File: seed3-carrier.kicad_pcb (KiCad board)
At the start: 2 copper layers, 113 x 61.6 mm, 47 parts, among them J1 AudioJack2, J2 AudioJack2, J3 5V_IN, J4 DISPLAY_UART, J5 SJ1-3535NG, J6 Seed3_PINS_RIGHT, J7 Seed3_PINS_LEFT, U1 TLV9062IDR, U2 TPA6111A2DR

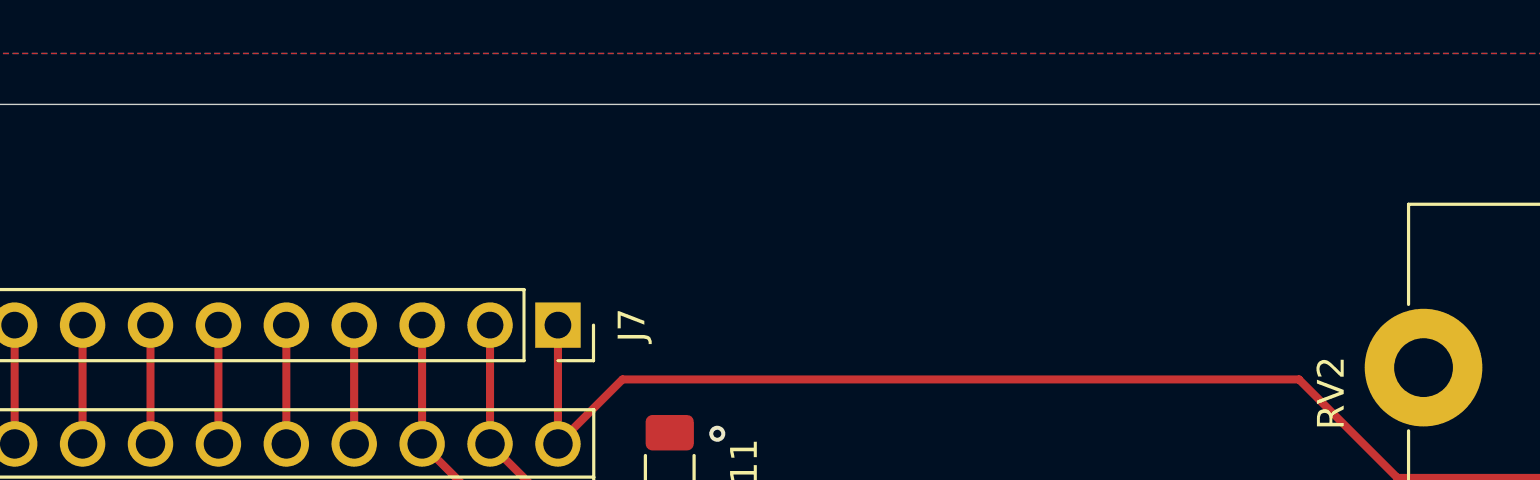
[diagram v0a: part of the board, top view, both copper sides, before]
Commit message: Add board revision, designer credits, and date to silkscreen
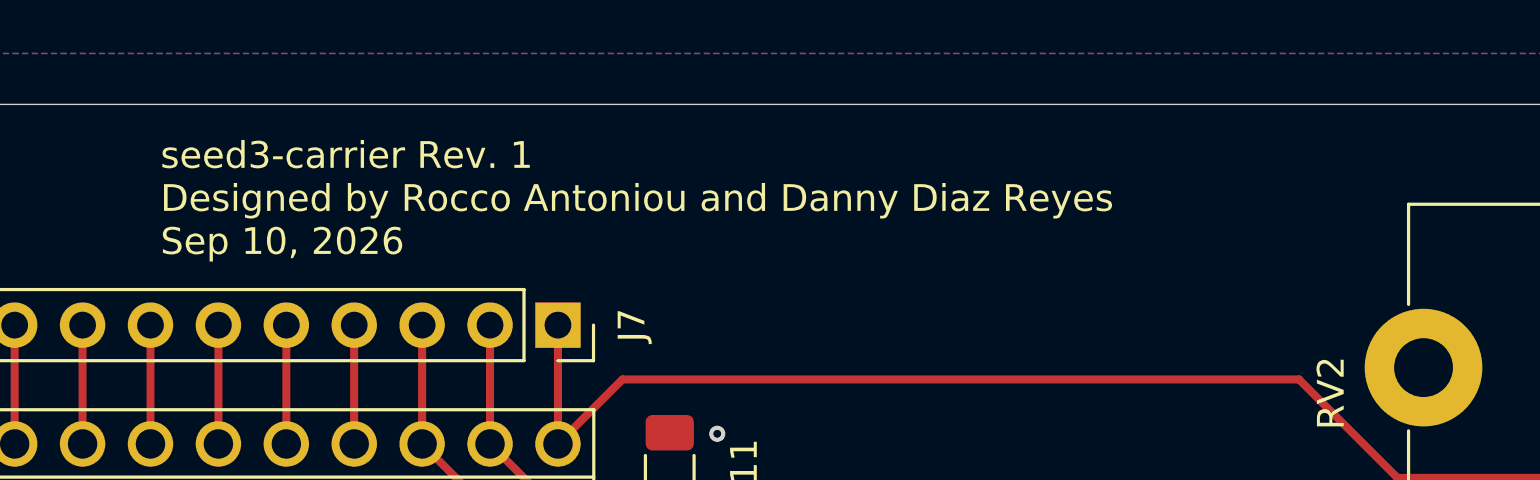
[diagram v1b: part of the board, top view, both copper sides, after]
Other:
- board text added: "seed3-carrier Rev. 1 Designed by Rocco Antoniou and Danny Diaz Reyes Sep 10, 2026"
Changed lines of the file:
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@@
+		)
+	)
+	(gr_text "seed3-carrier Rev. 1\nDesigned by Rocco Antoniou and Danny Diaz Reyes\nSep 10, 2026\n"
+		(at 86.106 45.72 0)
+		(layer "F.SilkS")
+		(effects
+			(font
+				(size 1 1)
+				(thickness 0.1)
+			)
+			(justify left bottom)
 		)
 	)

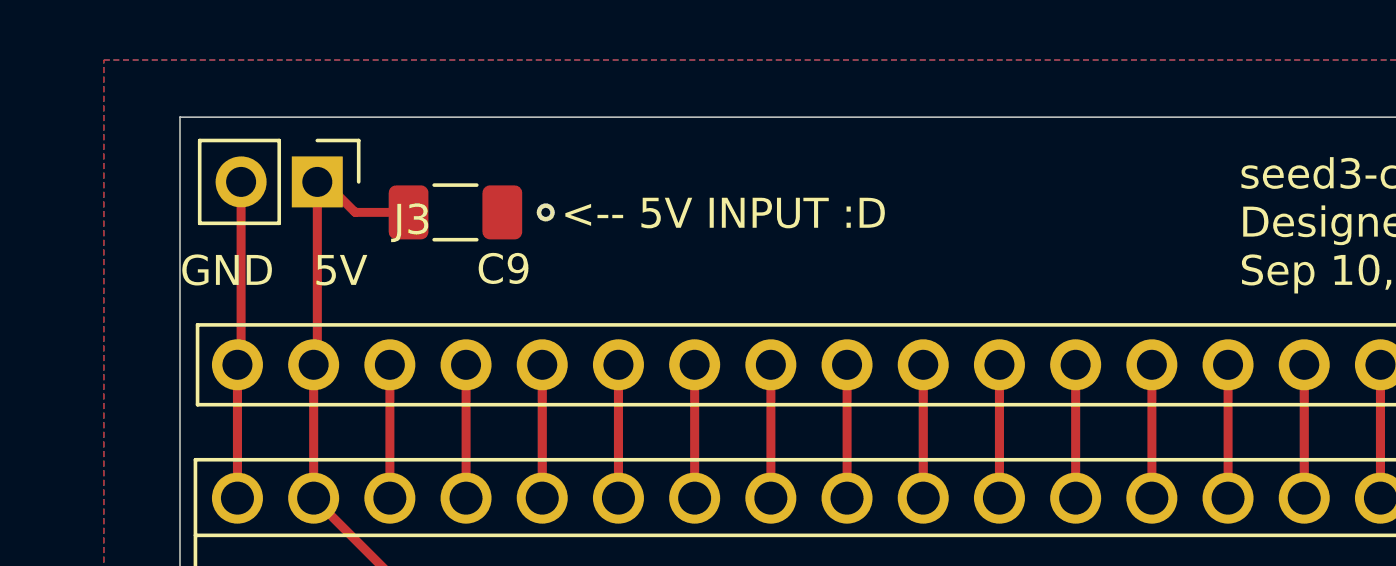
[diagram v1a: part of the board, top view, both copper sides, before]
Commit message: Add reverse-polarity protection and switched input mute
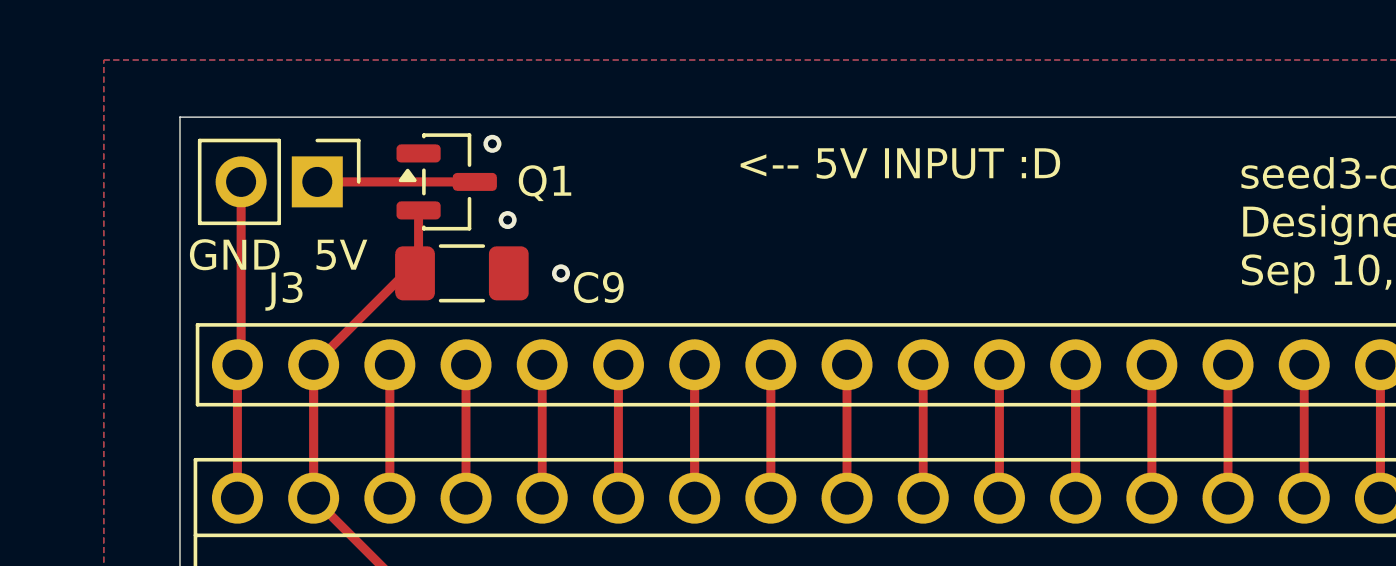
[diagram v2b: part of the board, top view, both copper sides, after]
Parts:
- added Q1: AO3401A, Package_TO_SOT_SMD:SOT-23, F.Cu at (59.7, 42.2)
- J1: value AudioJack2 -> AudioJack2_Switch
- moved C9 2.04 mm to (60.2, 45.2)
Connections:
- J1 pad SN: (no net) -> unconnected-(J1-PadSN)
- J1 pad TN: (no net) -> GND
- J3 pad 1: +5V -> Net-(J3-Pin_1)
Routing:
- net Net-(J3-Pin_1): track 0.00 -> 5.25 mm
- net +5V: track 132.6 -> 129.8 mm
- net GND: vias 16 -> 18

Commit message: Expand display header to four pins with protected 5V
Preserve GND and UART pin assignments and add protected +5V on pin 4. Reposition and label the header, reroute UART connections, and complete the power route with a short bottom-layer crossing beneath the buffered audio input. Refill copper zones.
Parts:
- J4: footprint Connector_PinHeader_2.54mm:PinHeader_1x03_P2.54mm_Vertical -> Connector_PinHeader_2.54mm:PinHeader_1x04_P2.54mm_Vertical
- moved J4 2.92 mm to (79.0, 75.6)
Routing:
- net +5V: track 129.8 -> 142.0 mm, vias 2 -> 4
- net /DISPLAY_UART_RX: track 8.15 -> 9.59 mm
- net /DISPLAY_UART_TX: track 8.15 -> 9.59 mm
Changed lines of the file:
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@@
 		)
 	)
-	(footprint "Connector_PinHeader_2.54mm:PinHeader_1x03_P2.54mm_Vertical"
+	(footprint "Connector_PinHeader_2.54mm:PinHeader_1x04_P2.54mm_Vertical"
 		(layer "F.Cu")
-		(at 81.915 75.565 90)
-		(descr "Through hole straight pin header, 1x03, 2.54mm pitch, single row")
-		(tags "Through hole pin header THT 1x03 2.54mm single row")
+		(at 78.994 75.565 90)
+		(descr "Through hole straight pin header, 1x04, 2.54mm pitch, single row")
+		(tags "Through hole pin header THT 1x04 2.54mm single row")
 		(property "Reference" "J4"
-			(at 0 7.62 270)
+			(at 0 10.16 270)
 			(layer "F.SilkS")
 			(effects
@@
 			)
 		)
-		(property "Description" "Generic connector, single row, 01x03, script generated (kicad-library-utils/schlib/autogen/connector/)"
+		(property "Description" "Generic connector, single row, 01x04, script generated (kicad-library-utils/schlib/autogen/connector/)"
 			(at 0 0 90)
 			(layer "F.Fab")
@@
 			(unit
 				(name "A")
-				(pins "1" "2" "3")
+				(pins "1" "2" "3" "4")
 			)
 		)
@@
 		(fp_line
 			(start 1.38 1.27)
-			(end 1.38 6.46)
+			(end 1.38 9)
 			(stroke
 				(width 0.12)
@@
 		(fp_line
 			(start -1.38 1.27)
-			(end -1.38 6.46)
+			(end -1.38 9)
 			(stroke
 				(width 0.12)
@@
 		)
 		(fp_line
-			(start -1.38 6.46)
-			(end 1.38 6.46)
+			(start -1.38 9)
+			(end 1.38 9)
 			(stroke
 				(width 0.12)
@@
 		(fp_rect
 			(start -1.77 -1.77)
-			(end 1.77 6.85)
+			(end 1.77 9.39)
 			(stroke
 				(width 0.05)
@@
 		(fp_line
 			(start 1.27 -1.27)
-			(end 1.27 6.35)
+			(end 1.27 8.89)
 			(stroke
 				(width 0.1)
@@
 		)
 		(fp_line
-			(start 1.27 6.35)
-			(end -1.27 6.35)
+			(start 1.27 8.89)
+			(end -1.27 8.89)
 			(stroke
 				(width 0.1)
@@
 		)
 		(fp_line
-			(start -1.27 6.35)
+			(start -1.27 8.89)
 			(end -1.27 -0.635)
 			(stroke
@@
 		)
 		(fp_text user "${REFERENCE}"
-			(at 0 2.54 0)
+			(at 0 3.81 0)
 			(layer "F.Fab")
 			(effects
@@
 			(pintype "passive")
 		)
+		(pad "4" thru_hole circle
+			(at 0 7.62 90)
+			(size 1.7 1.7)
+			(drill 1)
+			(layers "*.Cu" "*.Mask")
+			(remove_unused_layers no)
+			(net "+5V")
+			(pinfunction "Pin_4_4")
+			(pintype "passive")
+		)
 		(embedded_fonts no)
-		(model "${KICAD10_3DMODEL_DIR}/Connector_PinHeader_2.54mm.3dshapes/PinHeader_1x03_P2.54mm_Vertical.step"
+		(model "${KICAD10_3DMODEL_DIR}/Connector_PinHeader_2.54mm.3dshapes/PinHeader_1x04_P2.54mm_Vertical.step"
 			(offset
 				(xyz 0 0 0)
@@
 	)
 	(gr_text "<-- 5V INPUT :D"
-		(at 69.342 42.164 0)
+		(at 65.532 42.672 0)
 		(layer "F.SilkS")
 		(effects
@@
 	)
 	(gr_text "GND"
-		(at 79.756 78.74 0)
+		(at 76.962 78.74 0)
 		(layer "F.SilkS")
 		(effects
@@
 	)
 	(gr_text "TX"
-		(at 83.82 77.47 270)
+		(at 81.026 77.47 270)
 		(layer "F.SilkS")
 		(effects
@@
 	)
 	(gr_text "RX"
-		(at 86.36 77.47 270)
+		(at 83.566 77.47 270)
+		(layer "F.SilkS")
+		(effects
+			(font
+				(size 1 1)
+				(thickness 0.1)
+			)
+			(justify left bottom)
+		)
+	)
+	(gr_text "5V"
+		(at 86.106 77.47 270)
 		(layer "F.SilkS")
 		(effects
@@
 	)
 	(segment
+		(start 89.662 75.692)
+		(end 89.535 75.692)
+		(width 0.3)
+		(layer "F.Cu")
+		(net "+5V")
+	)
+	(segment
 		(start 109.22 80.01)
 		(end 108.966 79.756)
@@
 	)
 	(segment
+		(start 91.948 75.692)
+		(end 96.3045 75.692)
+		(width 0.3)
+		(layer "F.Cu")
+		(net "+5V")
+	)
+	(segment
 		(start 112.115 66.395)
 		(end 113.03 66.395)
@@
 	)
 	(segment
+		(start 89.535 75.692)
+		(end 89.408 75.565)
+		(width 0.3)
+		(layer "F.Cu")
+		(net "+5V")
+	)
+	(segment
 		(start 55.255 52.705)
 		(end 67.32 64.77)
@@
 	)
 	(segment
+		(start 96.3045 75.692)
+		(end 98.0825 77.47)
+		(width 0.3)
+		(layer "F.Cu")
+		(net "+5V")
+	)
+	(segment
 		(start 98.0825 79.0975)
 		(end 98.995 80.01)
@@
 	)
 	(segment
+		(start 89.408 75.565)
+		(end 86.614 75.565)
+		(width 0.3)
+		(layer "F.Cu")
+		(net "+5V")
+	)
+	(segment
 		(start 108.966 78.232)
 		(end 108.585 77.851)
@@
 	)
 	(via
+		(at 89.662 75.692)
+		(size 0.6)
+		(drill 0.3)
+		(layers "F.Cu" "B.Cu")
+		(net "+5V")
+	)
+	(via
 		(at 109.22 80.01)
 		(size 0.6)
@@
 	)
 	(via
+		(at 91.948 75.692)
+		(size 0.6)
+		(drill 0.3)
+		(layers "F.Cu" "B.Cu")
+		(net "+5V")
+	)
+	(via
 		(at 112.014 81.28)
 		(size 0.6)
@@
 	)
 	(segment
+		(start 89.662 75.692)
+		(end 91.948 75.692)
+		(width 0.3)
+		(layer "B.Cu")
+		(net "+5V")
+	)
+	(segment
 		(start 106.045 80.3025)
 		(end 102.2475 80.3025)
@@
 	)
 	(segment
-		(start 88.275 74.285)
-		(end 86.995 75.565)
+		(start 84.074 75.565)
+		(end 87.884 71.755)
 		(width 0.3)
 		(layer "F.Cu")
@@
 	)
 	(segment
-		(start 88.275 71.755)
-		(end 88.275 74.285)
+		(start 87.884 71.755)
+		(end 88.275 71.755)
 		(width 0.3)
 		(layer "F.Cu")
@@
 	)
 	(segment
-		(start 85.735 74.285)
-		(end 84.455 75.565)
+		(start 85.344 71.755)
+		(end 85.735 71.755)
 		(width 0.3)
 		(layer "F.Cu")
@@
 	)
 	(segment
-		(start 85.735 71.755)
-		(end 85.735 74.285)
+		(start 85.735 67.945)
+		(end 85.735 71.755)
 		(width 0.3)
 		(layer "F.Cu")
@@
 	)
 	(segment
-		(start 85.735 67.945)
-		(end 85.735 71.755)
+		(start 81.534 75.565)
+		(end 85.344 71.755)
 		(width 0.3)
 		(layer "F.Cu")
@@
 	)
 	(segment
+		(start 55.377 42.164)
+		(end 60.6275 42.164)
+		(width 0.3)
+		(layer "F.Cu")
+		(net "Net-(J3-Pin_1)")
+	)
+	(segment
 		(start 141.325 87.985)
 		(end 141.96 88.62)
@@
 		(net "Net-(C15-Pad2)")
 	)
-	(segment
-		(start 55.377 42.164)
-		(end 60.6275 42.164)
-		(width 0.3)
-		(layer "F.Cu")
-		(net "Net-(J3-Pin_1)")
-	)
 	(zone

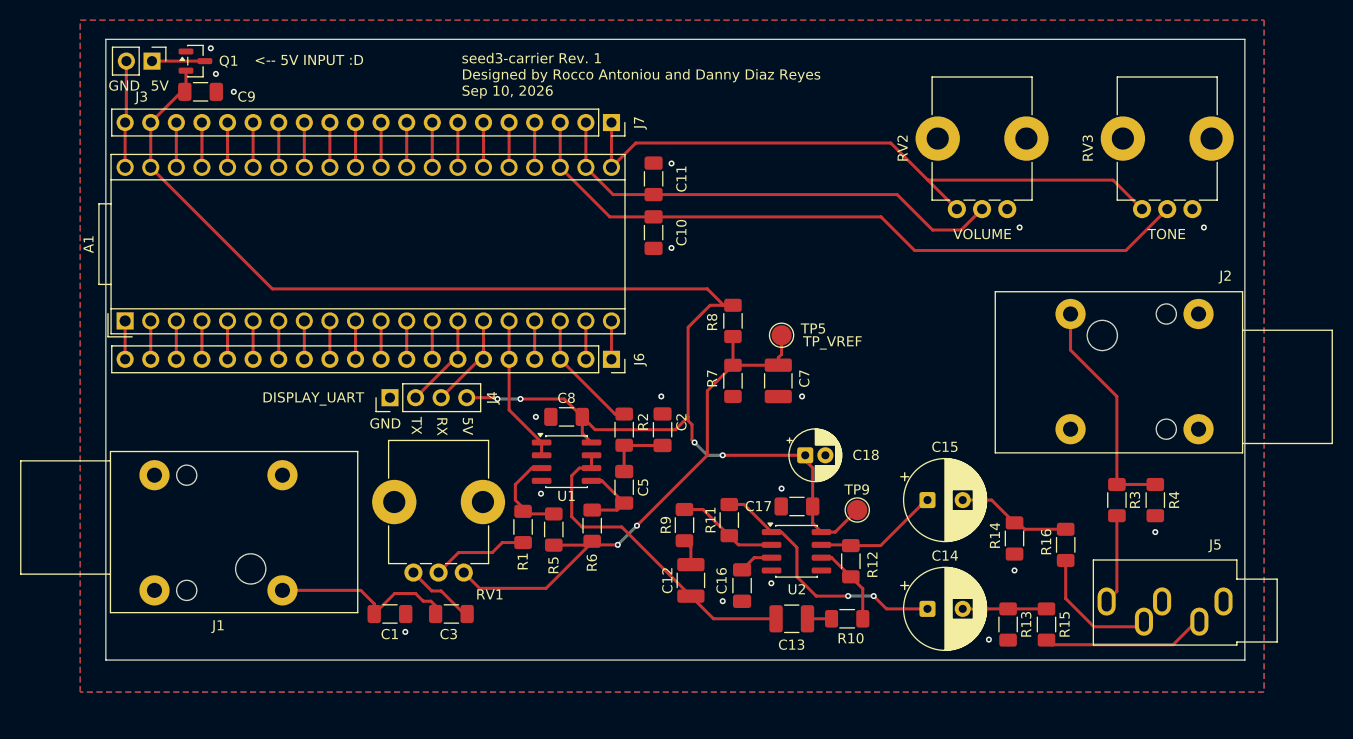
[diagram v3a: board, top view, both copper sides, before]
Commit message: Improve silkscreen labels and use 0.15 mm text strokes
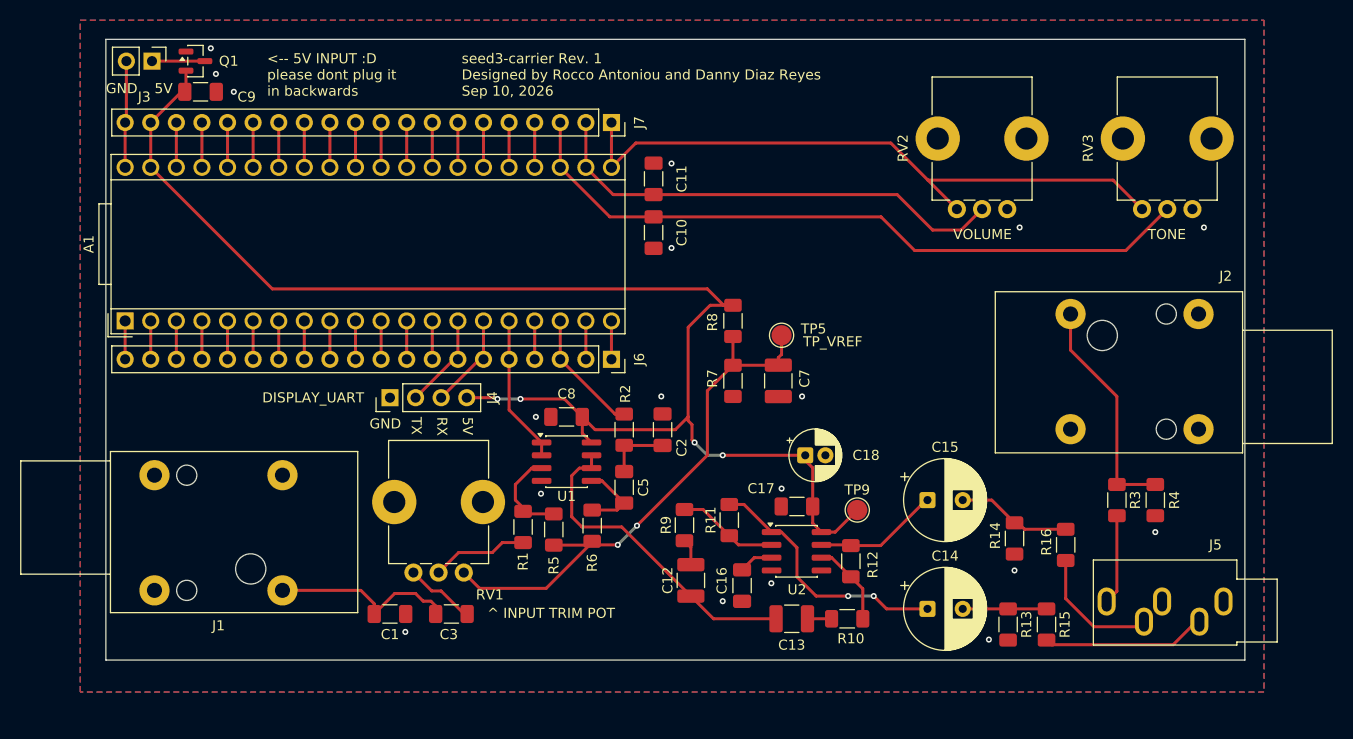
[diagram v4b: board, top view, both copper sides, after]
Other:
- board text added: "<-- 5V INPUT :D please dont plug it in backwards"
- board text added: "^ INPUT TRIM POT"
- board text removed: "<-- 5V INPUT :D"
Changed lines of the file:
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@@
 		(tags "capacitor handsolder")
 		(property "Reference" "C17"
-			(at 3.81 0 0)
+			(at 3.556 1.778 0)
 			(layer "F.SilkS")
 			(effects
@@
 		(tags "capacitor handsolder")
 		(property "Reference" "C2"
-			(at 0.762 1.905 90)
+			(at -1.778 1.905 90)
 			(layer "F.SilkS")
 			(effects
@@
 		(tags "resistor handsolder")
 		(property "Reference" "R2"
-			(at 0.762 1.905 90)
+			(at 3.556 0.127 90)
 			(layer "F.SilkS")
 			(effects
@@
 		(tags "Through hole pin header THT 1x02 2.54mm single row")
 		(property "Reference" "J3"
-			(at 3.556 1.021 0)
+			(at 3.556 0.767 0)
 			(layer "F.SilkS")
 			(effects
@@
 		(tags "capacitor handsolder")
 		(property "Reference" "C8"
-			(at 0 -1.85 0)
+			(at 0 -2.286 0)
 			(layer "F.SilkS")
 			(effects
@@
 	)
 	(gr_text "GND"
-		(at 51.054 45.212 0)
+		(at 50.8 45.466 0)
 		(layer "F.SilkS")
 		(effects
 			(font
 				(size 1 1)
-				(thickness 0.1)
+				(thickness 0.15)
 			)
 			(justify left bottom)
@@
 	)
 	(gr_text "5V"
-		(at 55.245 45.212 0)
+		(at 55.626 45.466 0)
 		(layer "F.SilkS")
 		(effects
 			(font
 				(size 1 1)
-				(thickness 0.1)
+				(thickness 0.15)
 			)
 			(justify left bottom)
 		)
 	)
-	(gr_text "<-- 5V INPUT :D"
-		(at 65.532 42.672 0)
+	(gr_text "<-- 5V INPUT :D\nplease dont plug it \nin backwards"
+		(at 66.802 45.72 0)
 		(layer "F.SilkS")
 		(effects
 			(font
 				(size 1 1)
-				(thickness 0.1)
+				(thickness 0.15)
 			)
 			(justify left bottom)
@@
 			(font
 				(size 1 1)
-				(thickness 0.1)
+				(thickness 0.15)
 			)
 			(justify left bottom)
@@
 			(font
 				(size 1 1)
-				(thickness 0.1)
+				(thickness 0.15)
+			)
+			(justify left bottom)
+		)
+	)
+	(gr_text "^ INPUT TRIM POT"
+		(at 88.646 97.536 0)
+		(layer "F.SilkS")
+		(effects
+			(font
+				(size 1 1)
+				(thickness 0.15)
 			)
 			(justify left bottom)
@@
 			(font
 				(size 1 1)
-				(thickness 0.1)
+				(thickness 0.15)
 			)
 			(justify left bottom)
@@
 			(font
 				(size 1 1)
-				(thickness 0.1)
+				(thickness 0.15)
 			)
 			(justify left bottom)
@@
 			(font
 				(size 1 1)
-				(thickness 0.1)
+				(thickness 0.15)
 			)
 			(justify left bottom)
@@
 			(font
 				(size 1 1)
-				(thickness 0.1)
+				(thickness 0.15)
 			)
 			(justify left bottom)
@@
 			(font
 				(size 1 1)
-				(thickness 0.1)
+				(thickness 0.15)
 			)
 			(justify left bottom)

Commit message: Move C14
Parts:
- moved C14 1.65 mm to (130.7, 96.5)
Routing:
- net Net-(U2-VOUT1): track 25.7 -> 24.0 mm
- net Net-(C14-Pad2): track 8.31 -> 9.96 mm
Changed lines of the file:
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@@
 	(footprint "Capacitor_THT:CP_Radial_D8.0mm_P3.50mm"
 		(layer "F.Cu")
-		(at 132.332349 96.52)
+		(at 130.681349 96.52)
 		(descr "CP, Radial series, Radial, pin pitch=3.50mm, diameter=8mm, height=12mm, Electrolytic Capacitor")
 		(tags "CP Radial series Radial pin pitch 3.50mm diameter 8mm height 12mm Electrolytic Capacitor")
@@
 	)
 	(segment
-		(start 127 95.25)
-		(end 128.27 96.52)
+		(start 128.27 96.52)
+		(end 130.681349 96.52)
 		(width 0.3)
 		(layer "F.Cu")
@@
 	)
 	(segment
-		(start 128.27 96.52)
-		(end 132.332349 96.52)
+		(start 127 95.25)
+		(end 128.27 96.52)
 		(width 0.3)
 		(layer "F.Cu")
@@
 	)
 	(segment
-		(start 135.832349 96.52)
-		(end 140.335 96.52)
+		(start 140.335 96.52)
+		(end 144.145 96.52)
 		(width 0.3)
 		(layer "F.Cu")
@@
 	)
 	(segment
-		(start 140.335 96.52)
-		(end 144.145 96.52)
+		(start 134.181349 96.52)
+		(end 140.335 96.52)
 		(width 0.3)
 		(layer "F.Cu")
